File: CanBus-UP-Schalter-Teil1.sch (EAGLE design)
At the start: 8 parts, among them K1 36.11, K2 36.11, X1 MKDSN1,5/3-5,08, X2 MKDSN1,5/3-5,08

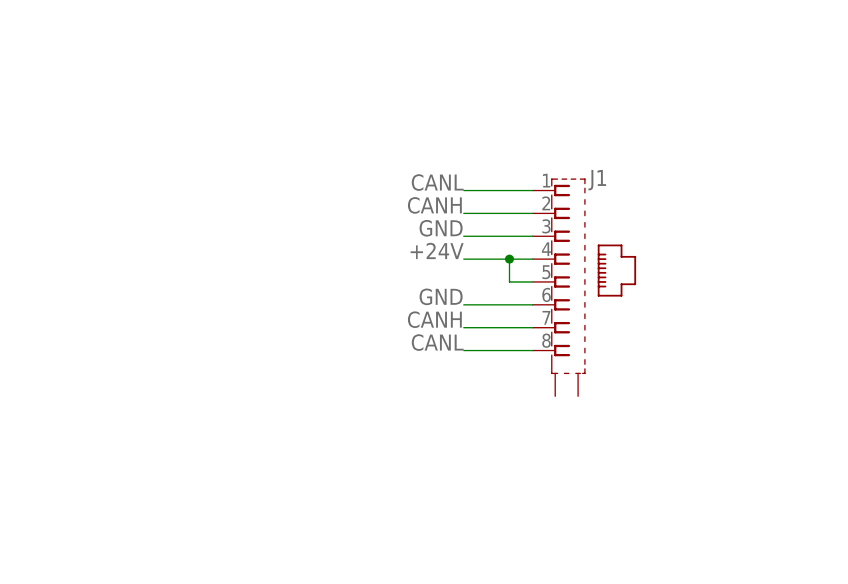
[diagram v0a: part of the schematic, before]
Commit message: CAN-Schield hinzugefügt, CanBus-UP-Schalter fertiggestellt
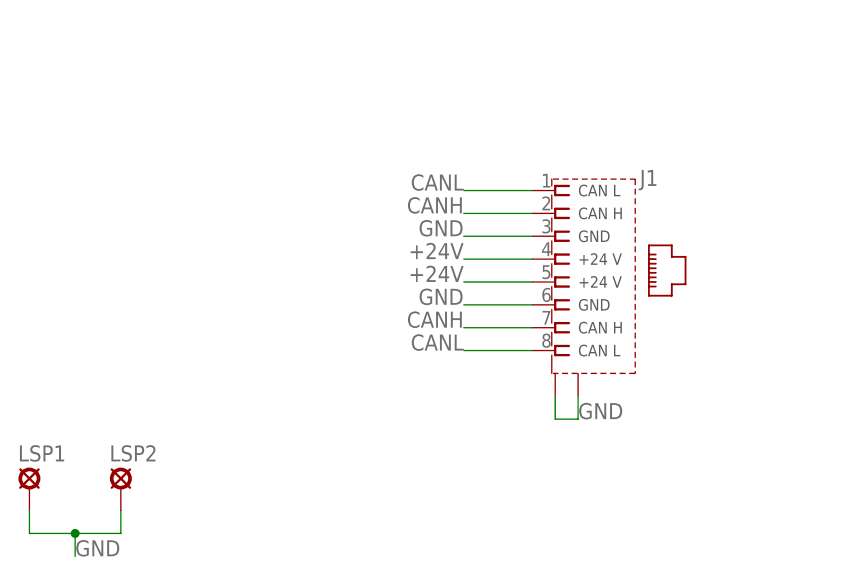
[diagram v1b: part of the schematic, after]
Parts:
- added LSP1, LSP2: LSP13, solpad:LSP13
- J1: device mebp_8-8g:555141-1 -> can-bus:RJ45-CAN
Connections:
- net GND: now also J1.S1, J1.S2, LSP1.MP, LSP2.MP
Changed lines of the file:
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@@
 <layer number="48" name="Document" color="7" fill="1" visible="no" active="no"/>
 <layer number="49" name="Reference" color="7" fill="1" visible="no" active="no"/>
+<layer number="50" name="dxf" color="7" fill="1" visible="no" active="no"/>
 <layer number="51" name="tDocu" color="7" fill="1" visible="no" active="no"/>
 <layer number="52" name="bDocu" color="7" fill="1" visible="no" active="no"/>
+<layer number="53" name="tGND_GNDA" color="7" fill="1" visible="no" active="no"/>
+<layer number="54" name="bGND_GNDA" color="7" fill="1" visible="no" active="no"/>
 <layer number="90" name="Modules" color="5" fill="1" visible="yes" active="yes"/>
 <layer number="91" name="Nets" color="2" fill="1" visible="yes" active="yes"/>
@@
 <layer number="98" name="Guide" color="6" fill="1" visible="yes" active="yes"/>
 <layer number="99" name="SpiceOrder" color="5" fill="1" visible="yes" active="yes"/>
+<layer number="100" name="Muster" color="7" fill="1" visible="yes" active="yes"/>
+<layer number="101" name="Flex-Kleb" color="7" fill="1" visible="yes" active="yes"/>
+<layer number="102" name="fp2" color="7" fill="1" visible="yes" active="yes"/>
+<layer number="103" name="fp3" color="7" fill="1" visible="yes" active="yes"/>
+<layer number="104" name="fp4" color="7" fill="1" visible="yes" active="yes"/>
+<layer number="105" name="Beschreib" color="7" fill="1" visible="yes" active="yes"/>
+<layer number="106" name="BGA-Top" color="7" fill="1" visible="yes" active="yes"/>
+<layer number="107" name="BD-Top" color="7" fill="1" visible="yes" active="yes"/>
+<layer number="108" name="fp8" color="7" fill="1" visible="yes" active="yes"/>
+<layer number="109" name="fp9" color="7" fill="1" visible="yes" active="yes"/>
+<layer number="110" name="fp0" color="7" fill="1" visible="yes" active="yes"/>
+<layer number="111" name="bdokum" color="7" fill="1" visible="yes" active="yes"/>
+<layer number="116" name="Patch_BOT" color="7" fill="1" visible="yes" active="yes"/>
+<layer number="121" name="tTestdril" color="7" fill="1" visible="yes" active="yes"/>
+<layer number="122" name="bTestdril" color="7" fill="1" visible="yes" active="yes"/>
+<layer number="123" name="tTestmark" color="7" fill="1" visible="yes" active="yes"/>
+<layer number="124" name="bTestmark" color="7" fill="1" visible="yes" active="yes"/>
+<layer number="125" name="tNamesSMD" color="7" fill="1" visible="yes" active="yes"/>
+<layer number="126" name="bNamesSMD" color="7" fill="1" visible="yes" active="yes"/>
+<layer number="127" name="tValueSMD" color="7" fill="1" visible="yes" active="yes"/>
+<layer number="128" name="bValueSMD" color="7" fill="1" visible="yes" active="yes"/>
+<layer number="131" name="tAdjust" color="7" fill="1" visible="yes" active="yes"/>
+<layer number="132" name="bAdjust" color="7" fill="1" visible="yes" active="yes"/>
+<layer number="151" name="tDocuSMD" color="7" fill="1" visible="yes" active="yes"/>
+<layer number="152" name="bDocuSMD" color="7" fill="1" visible="yes" active="yes"/>
+<layer number="199" name="Contour" color="7" fill="1" visible="yes" active="yes"/>
+<layer number="200" name="200bmp" color="7" fill="1" visible="yes" active="yes"/>
+<layer number="201" name="201bmp" color="7" fill="1" visible="yes" active="yes"/>
+<layer number="202" name="202bmp" color="7" fill="1" visible="yes" active="yes"/>
+<layer number="203" name="203bmp" color="7" fill="1" visible="yes" active="yes"/>
+<layer number="204" name="204bmp" color="7" fill="1" visible="yes" active="yes"/>
+<layer number="205" name="205bmp" color="7" fill="1" visible="yes" active="yes"/>
+<layer number="206" name="206bmp" color="7" fill="1" visible="yes" active="yes"/>
+<layer number="207" name="207bmp" color="7" fill="1" visible="yes" active="yes"/>
+<layer number="208" name="208bmp" color="7" fill="1" visible="yes" active="yes"/>
+<layer number="209" name="209bmp" color="7" fill="1" visible="yes" active="yes"/>
+<layer number="210" name="210bmp" color="7" fill="1" visible="yes" active="yes"/>
 <layer number="250" name="Descript" color="3" fill="1" visible="no" active="no"/>
 <layer number="251" name="SMDround" color="12" fill="11" visible="no" active="no"/>
+<layer number="254" name="OrgLBR" color="7" fill="1" visible="yes" active="yes"/>
 </layers>
 <schematic xreflabel="%F%N/%S.%C%R" xrefpart="/%S.%C%R">
@@
 </classes>
 <parts>
-<part name="J1" library="mebp_8-8g" deviceset="555141-1" device=""/>
+<part name="J1" library="can-bus" deviceset="RJ45-CAN" device=""/>
 <part name="K1" library="relay_finder_36_11" deviceset="36.11" device=""/>
 <part name="K2" library="relay_finder_36_11" deviceset="36.11" device=""/>
@@
 <part name="D2" library="diode" deviceset="DIODE-" device="SOD323-R"/>
 <part name="SV1" library="con-lsta" deviceset="FE06-1" device=""/>
+<part name="LSP1" library="solpad" deviceset="LSP13" device=""/>
+<part name="LSP2" library="solpad" deviceset="LSP13" device=""/>
 </parts>
 <sheets>
@@
 </plain>
 <instances>
-<instance part="J1" gate="G$1" x="78.74" y="63.5"/>
+<instance part="J1" gate="G$1" x="86.36" y="63.5"/>
 <instance part="K1" gate="G$1" x="162.56" y="101.6"/>
 <instance part="K2" gate="G$1" x="162.56" y="60.96"/>
@@
 <instance part="D2" gate="G$1" x="137.16" y="60.96" rot="R90"/>
 <instance part="SV1" gate="G$1" x="27.94" y="106.68"/>
+<instance part="LSP1" gate="1" x="20.32" y="40.64"/>
+<instance part="LSP2" gate="1" x="30.48" y="40.64"/>
 </instances>
 <busses>
@@
 <segment>
 <pinref part="J1" gate="G$1" pin="4"/>
-<wire x1="76.2" y1="66.04" x2="73.66" y2="66.04" width="0.1524" layer="91"/>
-<pinref part="J1" gate="G$1" pin="5"/>
-<wire x1="76.2" y1="63.5" x2="73.66" y2="63.5" width="0.1524" layer="91"/>
-<wire x1="73.66" y1="63.5" x2="73.66" y2="66.04" width="0.1524" layer="91"/>
-<junction x="73.66" y="66.04"/>
-<wire x1="73.66" y1="66.04" x2="68.58" y2="66.04" width="0.1524" layer="91"/>
+<wire x1="76.2" y1="66.04" x2="68.58" y2="66.04" width="0.1524" layer="91"/>
 <label x="68.58" y="66.04" size="1.778" layer="95" rot="MR0"/>
 </segment>
@@
 <label x="40.64" y="109.22" size="1.778" layer="95"/>
 </segment>
+<segment>
+<pinref part="J1" gate="G$1" pin="5"/>
+<wire x1="76.2" y1="63.5" x2="68.58" y2="63.5" width="0.1524" layer="91"/>
+<label x="68.58" y="63.5" size="1.778" layer="95" rot="MR0"/>
+</segment>
 </net>
 <net name="GND" class="0">
@@
 <label x="40.64" y="106.68" size="1.778" layer="95"/>
 </segment>
-</net>
+<segment>
+<pinref part="LSP1" gate="1" pin="MP"/>
+<wire x1="20.32" y1="38.1" x2="20.32" y2="35.56" width="0.1524" layer="91"/>
+<pinref part="LSP2" gate="1" pin="MP"/>
+<wire x1="20.32" y1="35.56" x2="25.4" y2="35.56" width="0.1524" layer="91"/>
+<wire x1="25.4" y1="35.56" x2="30.48" y2="35.56" width="0.1524" layer="91"/>
+<wire x1="30.48" y1="35.56" x2="30.48" y2="38.1" width="0.1524" layer="91"/>
+<wire x1="25.4" y1="35.56" x2="25.4" y2="33.02" width="0.1524" layer="91"/>
+<junction x="25.4" y="35.56"/>
+<label x="25.4" y="33.02" size="1.778" layer="95"/>
+</segment>
+<segment>
+<label x="81.28" y="48.26" size="1.778" layer="95"/>
+<pinref part="J1" gate="G$1" pin="S2"/>
+<wire x1="81.28" y1="48.26" x2="81.28" y2="50.8" width="0.1524" layer="91"/>
+<pinref part="J1" gate="G$1" pin="S1"/>
+<wire x1="78.74" y1="50.8" x2="78.74" y2="48.26" width="0.1524" layer="91"/>
+<wire x1="78.74" y1="48.26" x2="81.28" y2="48.26" width="0.1524" layer="91"/>
+</segment>
+</net>

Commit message: CanBus-UP-Schalter fertiggestellt
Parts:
- removed J1: (no value), can-bus:RJ45-CAN
- added LSP3, LSP4, LSP5, LSP6: LSP13, solpad:LSP13
- added SV2: (no value), can-bus:ML10L
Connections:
- net +24V: now also LSP6.MP, SV2.4, SV2.5; no longer J1.4, J1.5
- net CANH: now also SV2.2, SV2.7; no longer J1.2, J1.7
- net CANL: now also SV2.1, SV2.8; no longer J1.1, J1.8
- net GND: now also LSP3.MP, LSP4.MP, LSP5.MP, SV2.3, SV2.6; no longer J1.3, J1.6, J1.S1, J1.S2
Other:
- moved on the sheet: D1, D2, SV1, X1-1, X1-2, X1-3, X2-1, X2-2, X2-3
